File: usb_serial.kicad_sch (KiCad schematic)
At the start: 23 parts, among them J2 USB_B_Micro, U4 CP2102N-Axx-xQFN20, U5 AZ1117-3.3, U6 74LCX541

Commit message: Sent to fab v3.0
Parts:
- C12, C17: DIGIKEY 2679-C0603X7R160-104MNETR-ND -> 2679-C0603X7R160-104MNE-CT-ND
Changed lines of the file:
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@@
       (effects (font (size 1.27 1.27)) hide)
     )
-    (property "DIGIKEY" "2679-C0603X7R160-104MNETR-ND" (at 119.38 110.49 0)
+    (property "DIGIKEY" "2679-C0603X7R160-104MNE-CT-ND" (at 119.38 110.49 0)
       (effects (font (size 1.27 1.27)) hide)
     )
@@
       (effects (font (size 1.27 1.27)) hide)
     )
-    (property "DIGIKEY" "2679-C0603X7R160-104MNETR-ND" (at 88.265 110.49 0)
+    (property "DIGIKEY" "2679-C0603X7R160-104MNE-CT-ND" (at 88.265 110.49 0)
       (effects (font (size 1.27 1.27)) hide)
     )

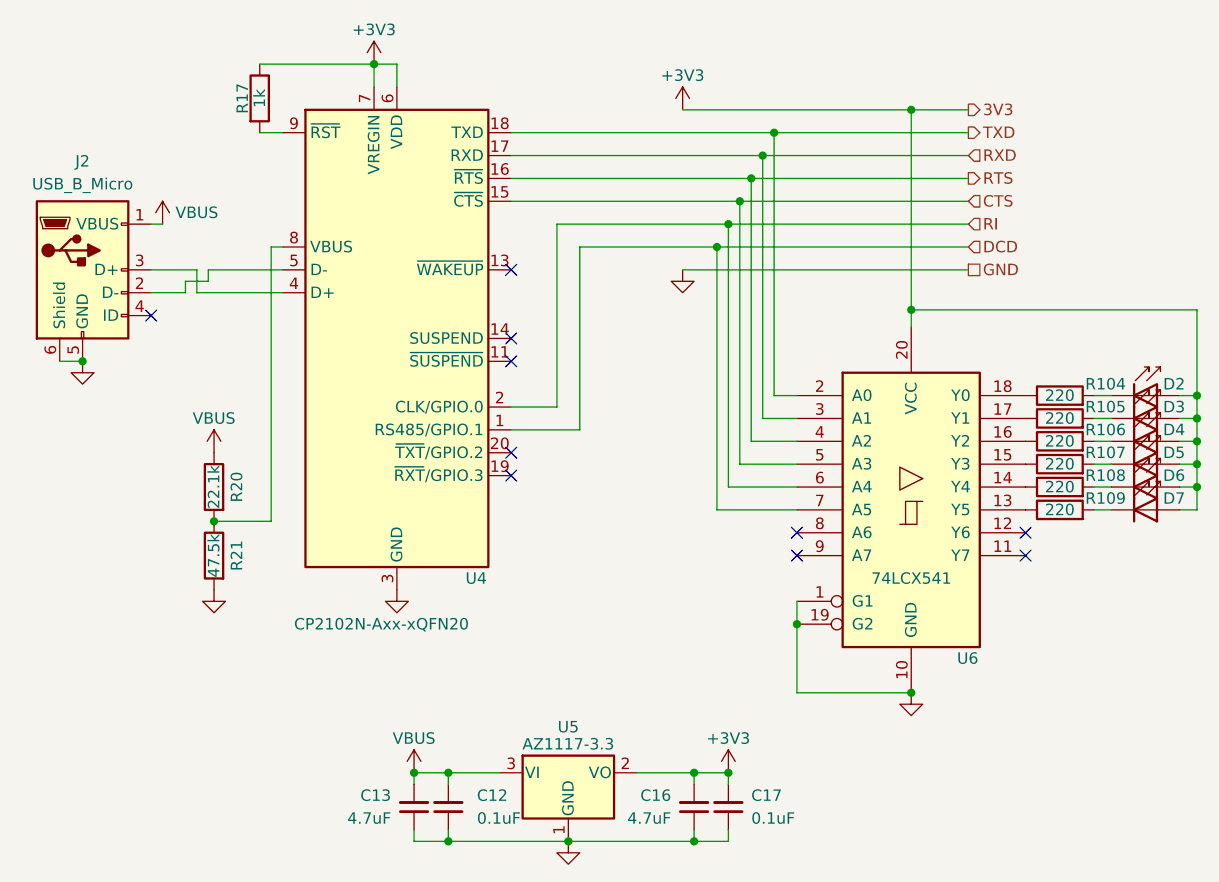
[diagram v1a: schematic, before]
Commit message: [4.0] M.2 Module. Sent to fab
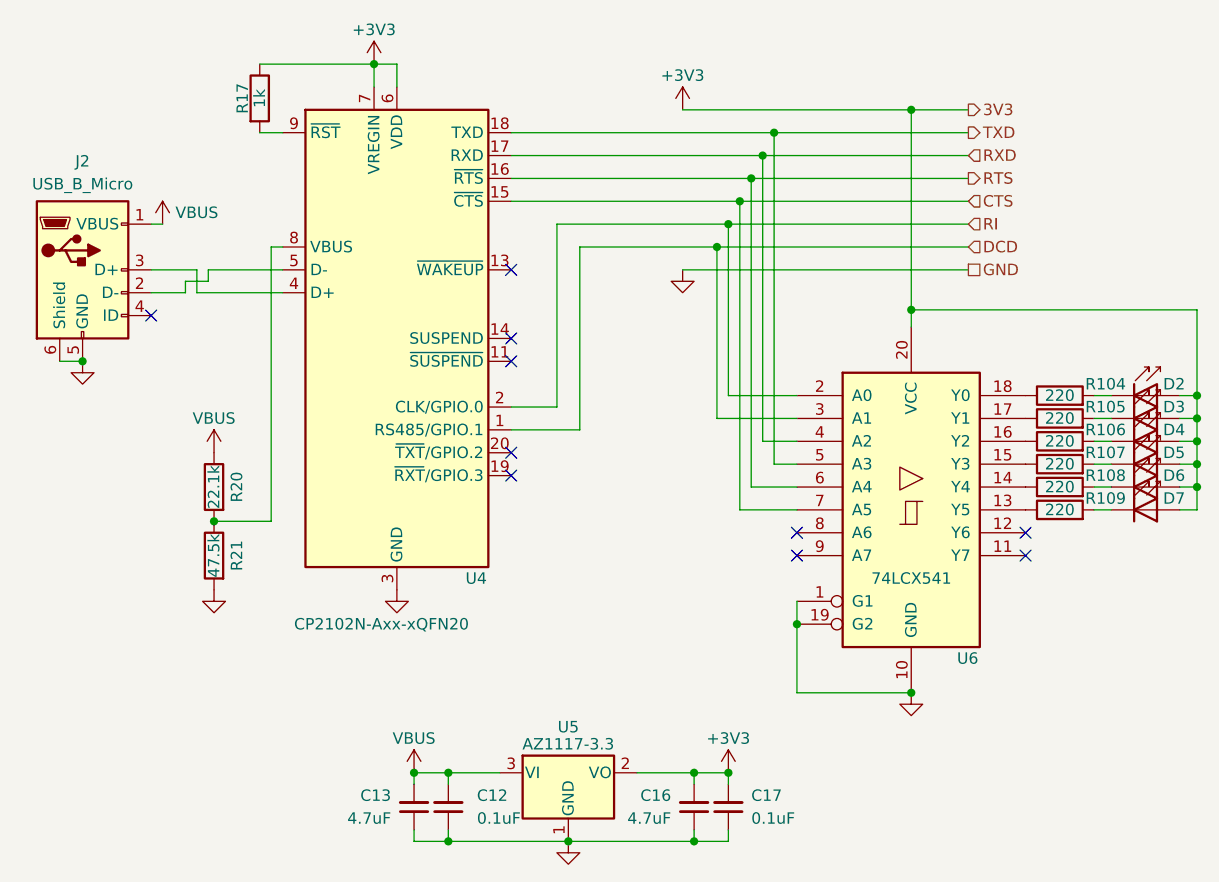
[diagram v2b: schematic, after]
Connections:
- net CTS: now also U6.7 (A5); no longer U6.5 (A3)
- net DCD: now also U6.3 (A1); no longer U6.7 (A5)
- net RI: now also U6.2 (A0); no longer U6.6 (A4)
- net RTS: now also U6.6 (A4); no longer U6.4 (A2)
- net RXD: now also U6.4 (A2); no longer U6.3 (A1)
- net TXD: now also U6.5 (A3); no longer U6.2 (A0)
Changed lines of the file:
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@@
 (kicad_sch (version 20230121) (generator eeschema)
-  (paper "A4")
+  (paper "USLetter")
   (title_block
     (title "SkyFax")
-    (date "2023-09-02")
-    (rev "3.0")
+    (date "2023-09-12")
+    (rev "4.0")
     (company "Brian Hong")
     (comment 1 "@im_eningeer")
@@
   (junction (at 171.45 67.31) (diameter 0) (color 0 0 0 0)
   )
+  (junction (at 124.46 35.56) (diameter 0) (color 0 0 0 0)
+  )
   (junction (at 171.45 64.77) (diameter 0) (color 0 0 0 0)
   )
@@
   (junction (at 88.265 114.3) (diameter 0) (color 0 0 0 0)
   )
+  (junction (at 119.38 45.72) (diameter 0) (color 0 0 0 0)
+  )
+  (junction (at 88.265 106.68) (diameter 0) (color 0 0 0 0)
+  )
+  (junction (at 139.7 97.79) (diameter 0) (color 0 0 0 0)
+  )
+  (junction (at 47.625 60.96) (diameter 0) (color 0 0 0 0)
+  )
+  (junction (at 62.23 78.74) (diameter 0) (color 0 0 0 0)
+  )
   (junction (at 123.19 38.1) (diameter 0) (color 0 0 0 0)
-  )
-  (junction (at 119.38 45.72) (diameter 0) (color 0 0 0 0)
-  )
-  (junction (at 88.265 106.68) (diameter 0) (color 0 0 0 0)
-  )
-  (junction (at 139.7 97.79) (diameter 0) (color 0 0 0 0)
-  )
-  (junction (at 124.46 35.56) (diameter 0) (color 0 0 0 0)
-  )
-  (junction (at 47.625 60.96) (diameter 0) (color 0 0 0 0)
-  )
-  (junction (at 62.23 78.74) (diameter 0) (color 0 0 0 0)
   )
   (junction (at 101.6 114.3) (diameter 0) (color 0 0 0 0)
@@
   (no_connect (at 127 80.01))
   (no_connect (at 152.4 80.01))
-  (wire (pts (xy 119.38 74.93) (xy 119.38 45.72))
-    (stroke (width 0) (type default))
-  )
-  (wire (pts (xy 124.46 35.56) (xy 124.46 64.77))
-    (stroke (width 0) (type default))
-  )
   (wire (pts (xy 171.45 67.31) (xy 171.45 64.77))
     (stroke (width 0) (type default))
   )
+  (wire (pts (xy 127 69.85) (xy 123.19 69.85))
+    (stroke (width 0) (type default))
+  )
   (wire (pts (xy 100.33 66.04) (xy 100.33 45.72))
     (stroke (width 0) (type default))
@@
     (stroke (width 0) (type default))
   )
-  (wire (pts (xy 146.05 35.56) (xy 124.46 35.56))
-    (stroke (width 0) (type default))
-  )
   (wire (pts (xy 59.055 52.07) (xy 61.595 52.07))
     (stroke (width 0) (type default))
@@
     (stroke (width 0) (type default))
   )
+  (wire (pts (xy 119.38 64.77) (xy 119.38 45.72))
+    (stroke (width 0) (type default))
+  )
   (wire (pts (xy 169.545 69.85) (xy 171.45 69.85))
     (stroke (width 0) (type default))
   )
+  (wire (pts (xy 118.11 67.31) (xy 127 67.31))
+    (stroke (width 0) (type default))
+  )
   (wire (pts (xy 88.265 106.68) (xy 93.98 106.68))
     (stroke (width 0) (type default))
@@
     (stroke (width 0) (type default))
   )
-  (wire (pts (xy 146.05 38.1) (xy 123.19 38.1))
-    (stroke (width 0) (type default))
-  )
   (wire (pts (xy 82.55 27.94) (xy 82.55 30.48))
     (stroke (width 0) (type default))
   )
-  (wire (pts (xy 127 64.77) (xy 124.46 64.77))
-    (stroke (width 0) (type default))
-  )
-  (wire (pts (xy 127 67.31) (xy 123.19 67.31))
+  (wire (pts (xy 124.46 72.39) (xy 127 72.39))
     (stroke (width 0) (type default))
   )
@@
     (stroke (width 0) (type default))
   )
+  (wire (pts (xy 127 77.47) (xy 120.65 77.47))
+    (stroke (width 0) (type default))
+  )
+  (wire (pts (xy 121.92 40.64) (xy 121.92 74.93))
+    (stroke (width 0) (type default))
+  )
   (wire (pts (xy 95.25 66.04) (xy 100.33 66.04))
     (stroke (width 0) (type default))
@@
     (stroke (width 0) (type default))
   )
-  (wire (pts (xy 121.92 69.85) (xy 121.92 40.64))
-    (stroke (width 0) (type default))
-  )
   (wire (pts (xy 102.87 68.58) (xy 95.25 68.58))
     (stroke (width 0) (type default))
@@
     (stroke (width 0) (type default))
   )
-  (wire (pts (xy 127 69.85) (xy 121.92 69.85))
+  (wire (pts (xy 120.65 43.18) (xy 120.65 77.47))
     (stroke (width 0) (type default))
   )
@@
     (stroke (width 0) (type default))
   )
-  (wire (pts (xy 127 72.39) (xy 120.65 72.39))
-    (stroke (width 0) (type default))
-  )
   (wire (pts (xy 102.87 48.26) (xy 118.11 48.26))
     (stroke (width 0) (type default))
@@
     (stroke (width 0) (type default))
   )
+  (wire (pts (xy 124.46 35.56) (xy 124.46 72.39))
+    (stroke (width 0) (type default))
+  )
+  (wire (pts (xy 118.11 48.26) (xy 118.11 67.31))
+    (stroke (width 0) (type default))
+  )
   (wire (pts (xy 60.325 50.8) (xy 60.325 53.34))
     (stroke (width 0) (type default))
@@
     (stroke (width 0) (type default))
   )
-  (wire (pts (xy 120.65 72.39) (xy 120.65 43.18))
+  (wire (pts (xy 124.46 35.56) (xy 146.05 35.56))
     (stroke (width 0) (type default))
   )
@@
     (stroke (width 0) (type default))
   )
-  (wire (pts (xy 123.19 67.31) (xy 123.19 38.1))
-    (stroke (width 0) (type default))
-  )
   (wire (pts (xy 100.33 45.72) (xy 119.38 45.72))
     (stroke (width 0) (type default))
   )
+  (wire (pts (xy 123.19 38.1) (xy 123.19 69.85))
+    (stroke (width 0) (type default))
+  )
   (wire (pts (xy 160.02 67.31) (xy 161.925 67.31))
     (stroke (width 0) (type default))
@@
     (stroke (width 0) (type default))
   )
+  (wire (pts (xy 123.19 38.1) (xy 146.05 38.1))
+    (stroke (width 0) (type default))
+  )
   (wire (pts (xy 127 87.63) (xy 127 90.17))
     (stroke (width 0) (type default))
@@
     (stroke (width 0) (type default))
   )
-  (wire (pts (xy 127 74.93) (xy 119.38 74.93))
-    (stroke (width 0) (type default))
-  )
   (wire (pts (xy 68.58 48.26) (xy 69.85 48.26))
     (stroke (width 0) (type default))
@@
     (stroke (width 0) (type default))
   )
+  (wire (pts (xy 121.92 74.93) (xy 127 74.93))
+    (stroke (width 0) (type default))
+  )
   (wire (pts (xy 68.58 78.74) (xy 68.58 48.26))
     (stroke (width 0) (type default))
   )
-  (wire (pts (xy 118.11 77.47) (xy 118.11 48.26))
-    (stroke (width 0) (type default))
-  )
   (wire (pts (xy 119.38 107.95) (xy 119.38 106.68))
     (stroke (width 0) (type default))
@@
     (stroke (width 0) (type default))
   )
+  (wire (pts (xy 119.38 64.77) (xy 127 64.77))
+    (stroke (width 0) (type default))
+  )
   (wire (pts (xy 56.515 45.72) (xy 55.245 45.72))
     (stroke (width 0) (type default))
@@
     (stroke (width 0) (type default))
   )
-  (wire (pts (xy 127 77.47) (xy 118.11 77.47))
-    (stroke (width 0) (type default))
-  )
